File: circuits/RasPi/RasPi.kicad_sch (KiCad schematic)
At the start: 6 parts, among them Q13 2N7002, Q20 2N7002, Q21 2N7002

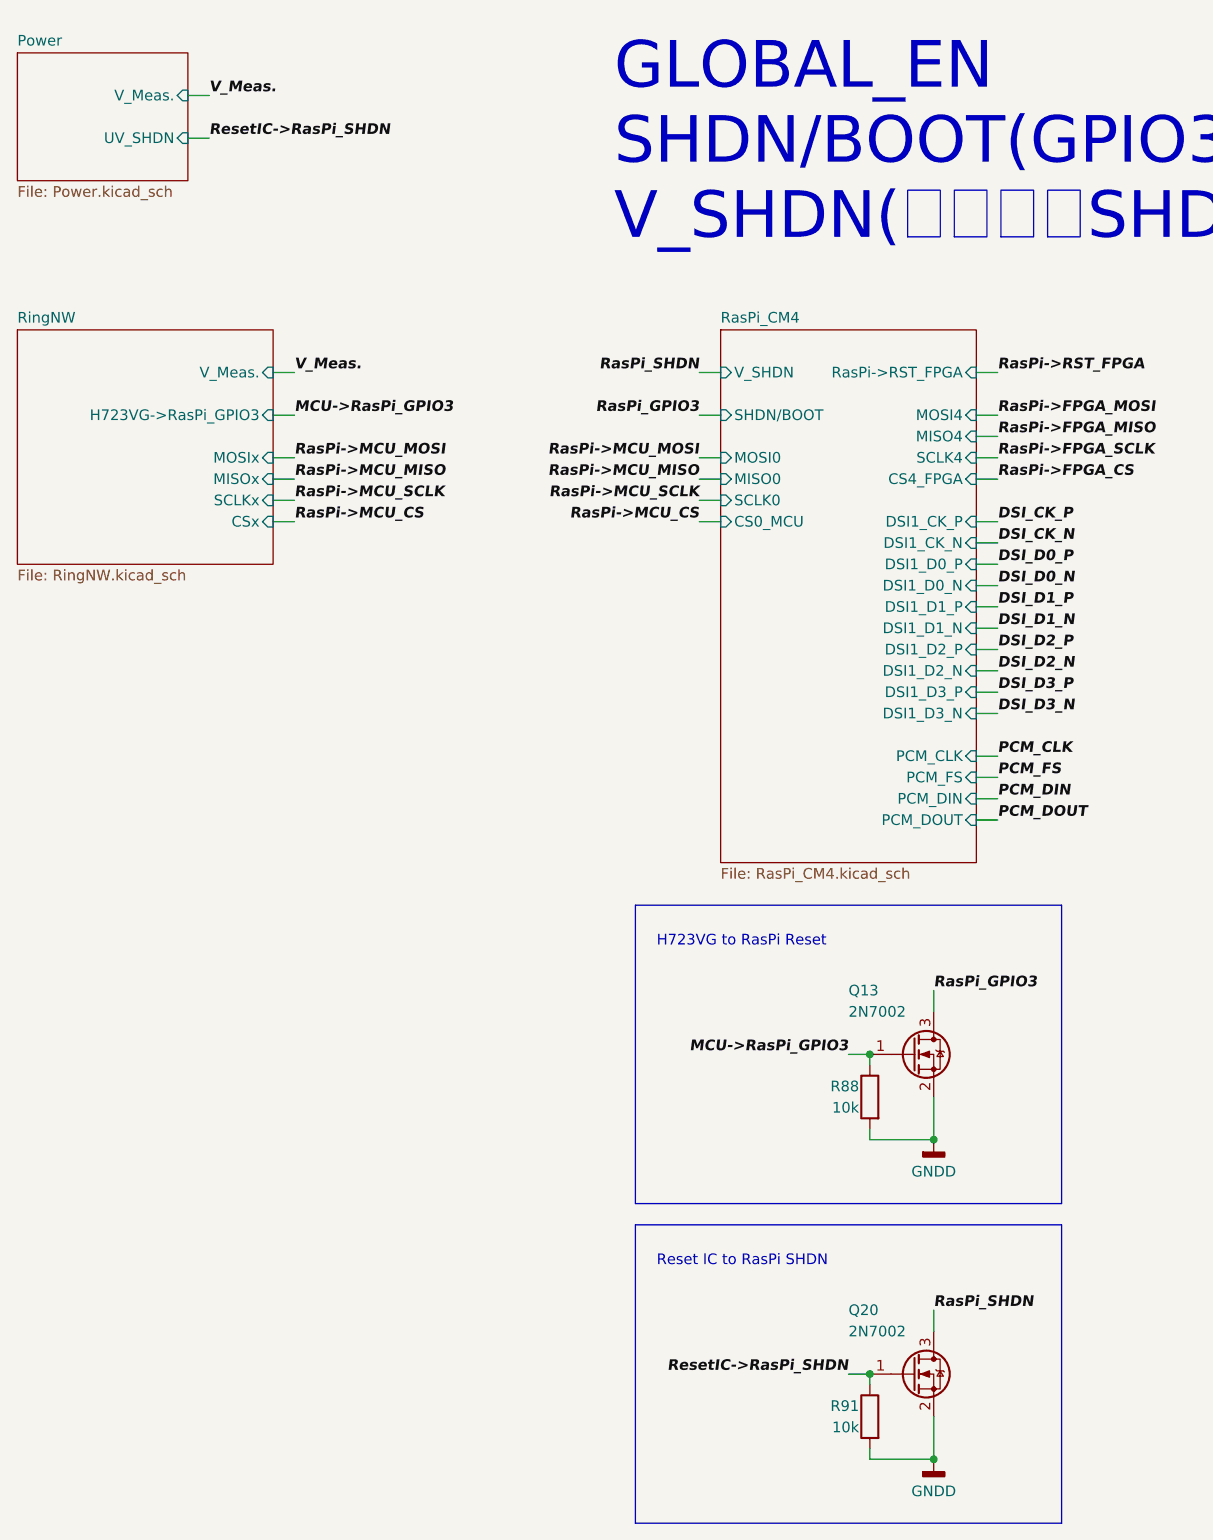
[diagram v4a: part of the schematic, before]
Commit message: 発注第2弾
RasPi発注
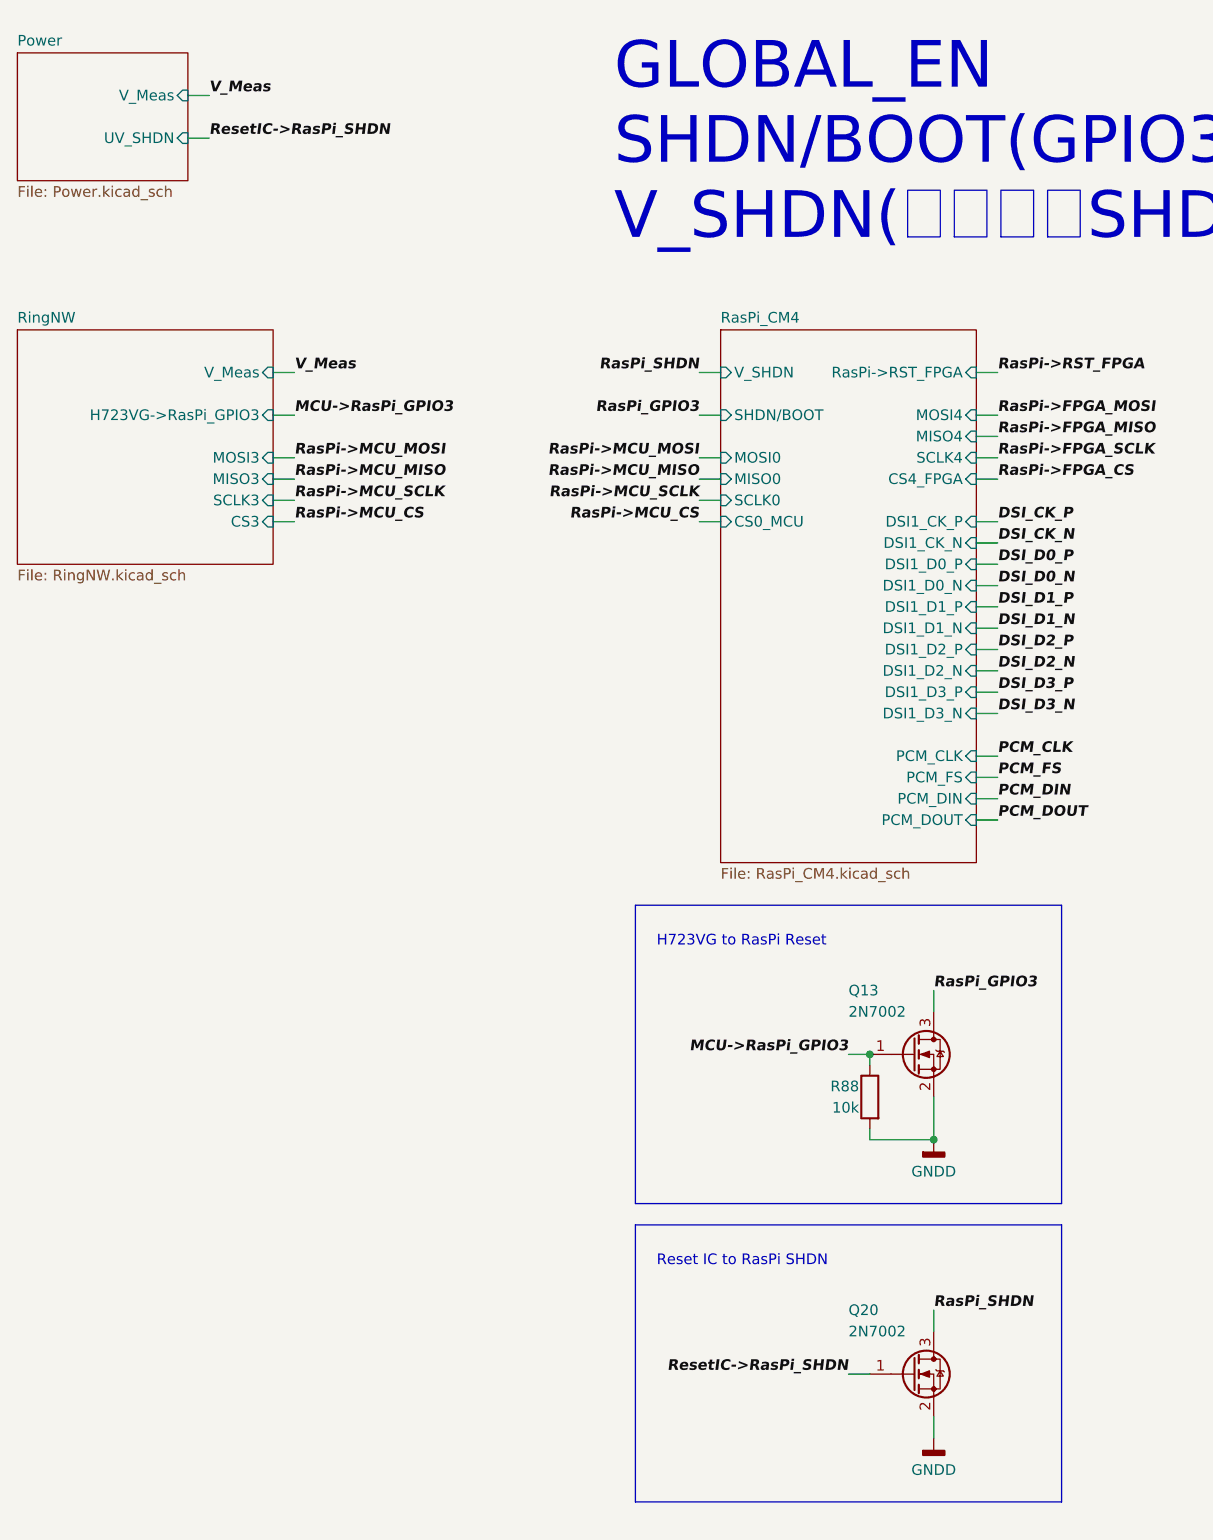
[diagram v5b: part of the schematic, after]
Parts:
- removed R91: 10k, Resistor_SMD:R_0402_1005Metric, symbol Device:R
- Q13, Q20: footprint Package_TO_SOT_SMD:SOT-23 -> Package_TO_SOT_SMD:SC-59
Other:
- sheet Power ports: added V_Meas; removed V_Meas.
- sheet RingNW ports: added CS3, MISO3, MOSI3, SCLK3, V_Meas; removed CSx, MISOx, MOSIx, SCLKx, V_Meas.
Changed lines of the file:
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@@
   (junction (at 152.4 137.16) (diameter 0) (color 0 0 0 0)
   )
-  (junction (at 160.02 185.42) (diameter 0) (color 0 0 0 0)
-  )
   (junction (at 160.02 147.32) (diameter 0) (color 0 0 0 0)
   )
-  (junction (at 152.4 175.26) (diameter 0) (color 0 0 0 0)
-  )
   (junction (at 233.68 137.16) (diameter 0) (color 0 0 0 0)
   )
@@
     (stroke (width 0) (type default))
   )
-  (wire (pts (xy 152.4 175.26) (xy 152.4 176.53))
-    (stroke (width 0) (type default))
-  )
   (wire (pts (xy 215.9 55.88) (xy 218.44 55.88))
     (stroke (width 0) (type default))
@@
     (stroke (width 0) (type default))
   )
-  (wire (pts (xy 152.4 185.42) (xy 160.02 185.42))
-    (stroke (width 0) (type default))
-  )
   (wire (pts (xy 167.64 96.52) (xy 165.1 96.52))
     (stroke (width 0) (type default))
@@
     (stroke (width 0) (type default))
   )
-  (wire (pts (xy 160.02 185.42) (xy 160.02 180.34))
+  (wire (pts (xy 160.02 182.88) (xy 160.02 180.34))
     (stroke (width 0) (type default))
   )
@@
     (stroke (width 0) (type default))
   )
-  (wire (pts (xy 152.4 184.15) (xy 152.4 185.42))
-    (stroke (width 0) (type default))
-  )
   (wire (pts (xy 215.9 101.6) (xy 218.44 101.6))
     (stroke (width 0) (type default))
@@
     (fill (type none))
   )
-  (rectangle (start 124.46 157.48) (end 175.26 193.04)
+  (rectangle (start 124.46 157.48) (end 175.26 190.5)
     (stroke (width 0) (type default))
     (fill (type none))
@@
     (effects (font (size 1.27 1.27) (thickness 0.254) bold italic) (justify left bottom))
   )
-  (label "V_Meas." (at 73.66 22.86 0) (fields_autoplaced)
+  (label "V_Meas" (at 73.66 22.86 0) (fields_autoplaced)
     (effects (font (size 1.27 1.27) (thickness 0.254) bold italic) (justify left bottom))
   )
@@
     (effects (font (size 1.27 1.27) (thickness 0.254) bold italic) (justify right bottom))
   )
-  (label "V_Meas." (at 83.82 55.88 0) (fields_autoplaced)
+  (label "V_Meas" (at 83.82 55.88 0) (fields_autoplaced)
     (effects (font (size 1.27 1.27) (thickness 0.254) bold italic) (justify left bottom))
   )
@@
       (effects (font (size 1.27 1.27)) (justify left))
     )
-    (property "Footprint" "Package_TO_SOT_SMD:SOT-23" (at 162.56 139.065 0)
+    (property "Footprint" "Package_TO_SOT_SMD:SC-59" (at 162.56 139.065 0)
       (effects (font (size 1.27 1.27) italic) (justify left) hide)
     )
@@
     )
   )
-  (symbol (lib_id "Device:R") (at 152.4 180.34 0) (mirror y) (unit 1)
-    (in_bom yes) (on_board yes) (dnp no)
-    (property "Reference" "R91" (at 151.13 179.07 0)
-      (effects (font (size 1.27 1.27)) (justify left))
-    )
-    (property "Value" "10k" (at 151.13 181.61 0)
-      (effects (font (size 1.27 1.27)) (justify left))
-    )
-    (property "Footprint" "Resistor_SMD:R_0402_1005Metric" (at 154.178 180.34 90)
-      (effects (font (size 1.27 1.27)) hide)
-    )
-    (property "Datasheet" "~" (at 152.4 180.34 0)
-      (effects (font (size 1.27 1.27)) hide)
-    )
-    (pin "1")
-    (pin "2")
-    (instances
-      (project "RasPi"
-        (path "/689a9e74-f202-4ea4-bfbb-4341f2549250"
-          (reference "R91") (unit 1)
-        )
-      )
-    )
-  )
   (symbol (lib_id "power:GNDD") (at 160.02 147.32 0) (unit 1)
     (in_bom yes) (on_board yes) (dnp no)
@@
       (effects (font (size 1.27 1.27)) (justify left))
     )
-    (property "Footprint" "Package_TO_SOT_SMD:SOT-23" (at 162.56 177.165 0)
+    (property "Footprint" "Package_TO_SOT_SMD:SC-59" (at 162.56 177.165 0)
       (effects (font (size 1.27 1.27) italic) (justify left) hide)
     )
@@
     )
   )
-  (symbol (lib_id "power:GNDD") (at 160.02 185.42 0) (unit 1)
-    (in_bom yes) (on_board yes) (dnp no)
-    (property "Reference" "#PWR097" (at 160.02 191.77 0)
-      (effects (font (size 1.27 1.27)) hide)
-    )
-    (property "Value" "GNDD" (at 160.02 189.23 0)
+  (symbol (lib_id "power:GNDD") (at 160.02 182.88 0) (unit 1)
+    (in_bom yes) (on_board yes) (dnp no)
+    (property "Reference" "#PWR097" (at 160.02 189.23 0)
+      (effects (font (size 1.27 1.27)) hide)
+    )
+    (property "Value" "GNDD" (at 160.02 186.69 0)
       (effects (font (size 1.27 1.27)))
     )
-    (property "Footprint" "" (at 160.02 185.42 0)
-      (effects (font (size 1.27 1.27)) hide)
-    )
-    (property "Datasheet" "" (at 160.02 185.42 0)
+    (property "Footprint" "" (at 160.02 182.88 0)
+      (effects (font (size 1.27 1.27)) hide)
+    )
+    (property "Datasheet" "" (at 160.02 182.88 0)
       (effects (font (size 1.27 1.27)) hide)
     )
@@
       (effects (font (size 1.27 1.27)) (justify left top))
     )
-    (pin "MISOx" input (at 81.28 68.58 0)
+    (pin "H723VG->RasPi_GPIO3" input (at 81.28 60.96 0)
       (effects (font (size 1.27 1.27)) (justify right))
     )
-    (pin "MOSIx" input (at 81.28 66.04 0)
+    (pin "V_Meas" input (at 81.28 55.88 0)
       (effects (font (size 1.27 1.27)) (justify right))
     )
-    (pin "SCLKx" input (at 81.28 71.12 0)
+    (pin "MOSI3" input (at 81.28 66.04 0)
       (effects (font (size 1.27 1.27)) (justify right))
     )
-    (pin "V_Meas." input (at 81.28 55.88 0)
+    (pin "MISO3" input (at 81.28 68.58 0)
       (effects (font (size 1.27 1.27)) (justify right))
     )
-    (pin "CSx" input (at 81.28 73.66 0)
+    (pin "SCLK3" input (at 81.28 71.12 0)
       (effects (font (size 1.27 1.27)) (justify right))
     )
-    (pin "H723VG->RasPi_GPIO3" input (at 81.28 60.96 0)
+    (pin "CS3" input (at 81.28 73.66 0)
       (effects (font (size 1.27 1.27)) (justify right))
     )
@@
       (effects (font (size 1.27 1.27)) (justify left top))
     )
-    (pin "V_Meas." input (at 71.12 22.86 0)
+    (pin "V_Meas" input (at 71.12 22.86 0)
       (effects (font (size 1.27 1.27)) (justify right))
     )
